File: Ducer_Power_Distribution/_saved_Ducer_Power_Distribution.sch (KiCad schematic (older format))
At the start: 12 parts, among them J1 Mini_Fit_Jr_1x3_pin, J10 Conn_01x05, J11 Power In, J2 Mini_Fit_Jr_1x3_pin, J3 Mini_Fit_Jr_1x3_pin, J4 Mini_Fit_Jr_1x3_pin, J5 Mini_Fit_Jr_1x3_pin, J6 Mini_Fit_Jr_1x3_pin, J7 Mini_Fit_Jr_1x3_pin, J8 Mini_Fit_Jr_1x3_pin, J9 Conn_01x05

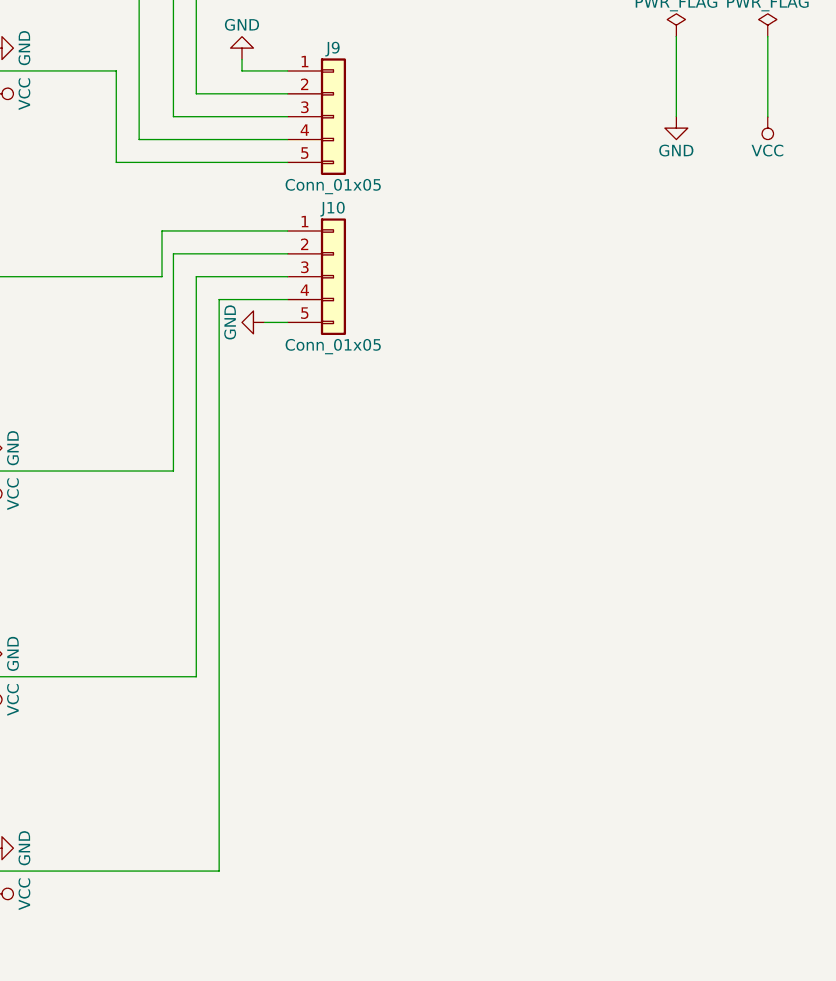
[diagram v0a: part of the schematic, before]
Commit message: Added aux port, mirrored layers
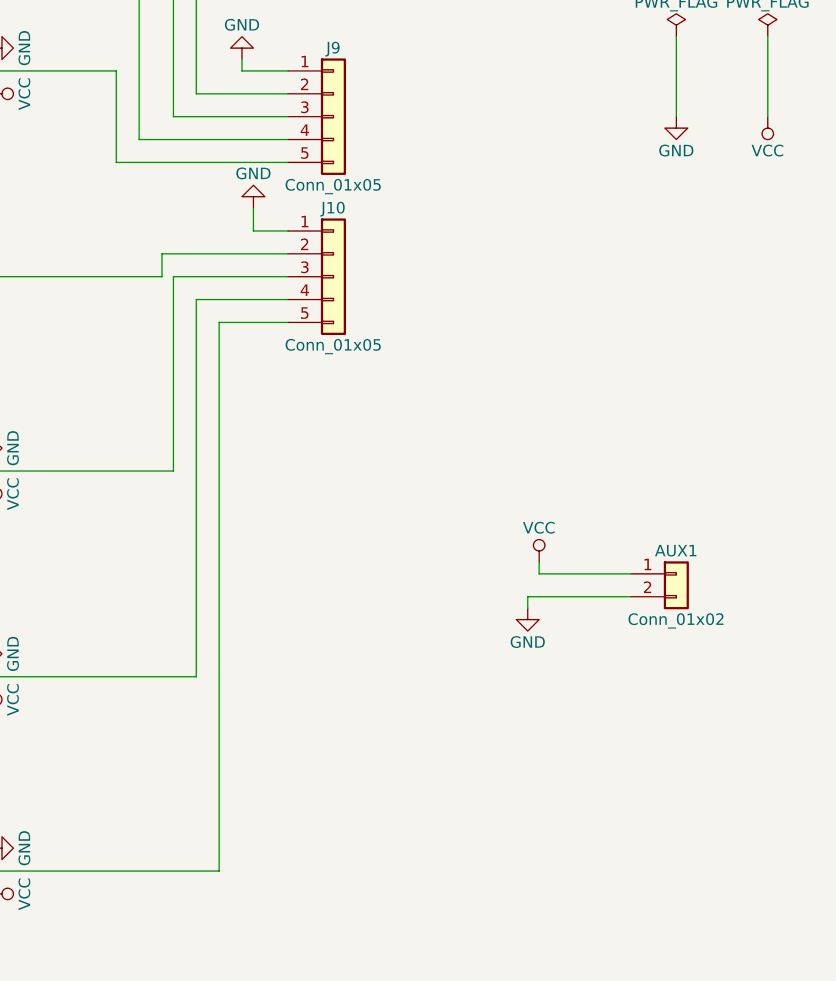
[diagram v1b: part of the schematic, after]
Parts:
- added AUX1: Conn_01x02, mylibrary:01x02_5mm_Screw_Terminals, symbol Conn_01x02
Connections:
- net GND: now also J10.1 (Pin_1), AUX1.2 (Pin_2); no longer J10.5 (Pin_5)
- net VCC: now also AUX1.1 (Pin_1)
- net at J5.2 (SIG): now also J10.2 (Pin_2); no longer J10.1 (Pin_1)
- net at J6.2 (SIG): now also J10.3 (Pin_3); no longer J10.2 (Pin_2)
- net at J7.2 (SIG): now also J10.4 (Pin_4); no longer J10.3 (Pin_3)
- net at J8.2 (SIG): now also J10.5 (Pin_5); no longer J10.4 (Pin_4)
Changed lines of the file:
@@
 	2800 4700 4000 4700
 Wire Wire Line
-	4000 4700 4000 4500
-Wire Wire Line
-	4000 4500 4550 4500
+	4000 4700 4000 4600
 Wire Wire Line
 	2800 5550 4050 5550
 Wire Wire Line
-	4050 5550 4050 4600
-Wire Wire Line
-	4050 4600 4550 4600
+	4050 5550 4050 4700
 Wire Wire Line
 	2800 6450 4150 6450
 Wire Wire Line
-	4150 6450 4150 4700
-Wire Wire Line
-	4150 4700 4550 4700
+	4150 6450 4150 4800
 Wire Wire Line
 	2800 7300 4250 7300
 Wire Wire Line
-	4250 7300 4250 4800
-Wire Wire Line
-	4250 4800 4550 4800
+	4250 7300 4250 4900
 Wire Wire Line
 	5750 1600 5750 1900
@@
 L GND #PWR021
 U 1 1 5AC16AC7
-P 4450 4900
-F 0 "#PWR021" H 4450 4650 50  0001 C CNN
-F 1 "GND" H 4450 4750 50  0000 C CNN
-F 2 "" H 4450 4900 50  0001 C CNN
-F 3 "" H 4450 4900 50  0001 C CNN
-	1    4450 4900
-	0    1    1    0
+P 4400 4400
+F 0 "#PWR021" H 4400 4150 50  0001 C CNN
+F 1 "GND" H 4400 4250 50  0000 C CNN
+F 2 "" H 4400 4400 50  0001 C CNN
+F 3 "" H 4400 4400 50  0001 C CNN
+	1    4400 4400
+	-1   0    0    1
 $EndComp
-Wire Wire Line
-	4550 4900 4450 4900
 $Comp
 L GND #PWR022
@@
 Wire Wire Line
 	4350 3800 4350 3750
+Wire Wire Line
+	4000 4600 4550 4600
+Wire Wire Line
+	4050 4700 4550 4700
+Wire Wire Line
+	4150 4800 4550 4800
+Wire Wire Line
+	4250 4900 4550 4900
+Wire Wire Line
+	4550 4500 4400 4500
+Wire Wire Line
+	4400 4500 4400 4400
+$Comp
+L Conn_01x02 AUX1
+U 1 1 5AC3C3DF
+P 6250 6000
+F 0 "AUX1" H 6250 6100 50  0000 C CNN
+F 1 "Conn_01x02" H 6250 5800 50  0000 C CNN
+F 2 "mylibrary:01x02_5mm_Screw_Terminals" H 6250 6000 50  0001 C CNN
+F 3 "" H 6250 6000 50  0001 C CNN
+	1    6250 6000
+	1    0    0    -1
+$EndComp
+$Comp
+L VCC #PWR027
+U 1 1 5AC3C462
+P 5650 5950
+F 0 "#PWR027" H 5650 5800 50  0001 C CNN
+F 1 "VCC" H 5650 6100 50  0000 C CNN
+F 2 "" H 5650 5950 50  0001 C CNN
+F 3 "" H 5650 5950 50  0001 C CNN
+	1    5650 5950
+	1    0    0    -1
+$EndComp
+$Comp
+L GND #PWR028
+U 1 1 5AC3C4AA
+P 5600 6150
+F 0 "#PWR028" H 5600 5900 50  0001 C CNN
+F 1 "GND" H 5600 6000 50  0000 C CNN
+F 2 "" H 5600 6150 50  0001 C CNN
+F 3 "" H 5600 6150 50  0001 C CNN
+	1    5600 6150
+	1    0    0    -1
+$EndComp
+Wire Wire Line
+	6050 6000 5650 6000
+Wire Wire Line
+	5650 6000 5650 5950
+Wire Wire Line
+	6050 6100 5600 6100
+Wire Wire Line
+	5600 6100 5600 6150
 $EndSCHEMATC
